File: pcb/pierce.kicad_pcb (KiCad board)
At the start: 2 copper layers, 227.3 x 105.6 mm, 100 parts, among them J1 Conn_01x12, J2 Conn_01x12, J3 Trackpoint, SW1 SW_PUSH, SW10 SW_PUSH, SW11 SW_PUSH, SW12 SW_PUSH, SW13 SW_PUSH, SW14 SW_PUSH, SW15 SW_PUSH, SW16 SW_PUSH, SW17 SW_PUSH, SW18 SW_PUSH, SW19 SW_PUSH, SW2 SW_PUSH, SW20 SW_PUSH, SW21 SW_PUSH, SW22 SW_PUSH, SW23 SW_PUSH, SW24 SW_PUSH, SW25 SW_PUSH, SW26 SW_PUSH, SW27 SW_PUSH, SW28 SW_PUSH, SW29 SW_PUSH, SW3 SW_PUSH, SW30 SW_PUSH, SW31 SW_PUSH, SW32 SW_PUSH, SW33 SW_PUSH, SW34 SW_PUSH, SW35 SW_PUSH, SW36 SW_PUSH, SW37 SW_PUSH, SW38 Rotary_Encoder, SW4 SW_PUSH, SW5 SW_PUSH, SW6 SW_PUSH, SW7 SW_PUSH, SW8 SW_PUSH, SW9 SW_PUSH, U1 Elite-C_reverse

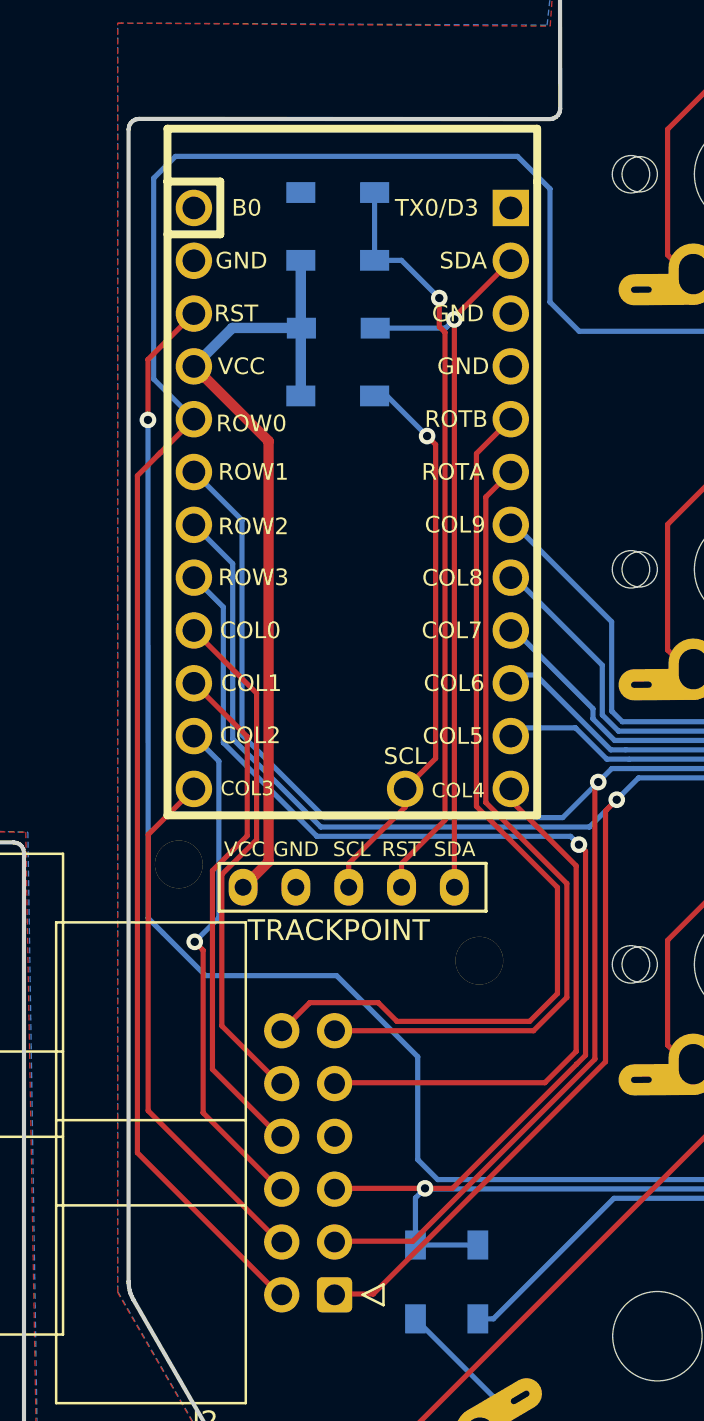
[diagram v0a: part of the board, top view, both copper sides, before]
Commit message: change pro micro footprint, smaller drill holes
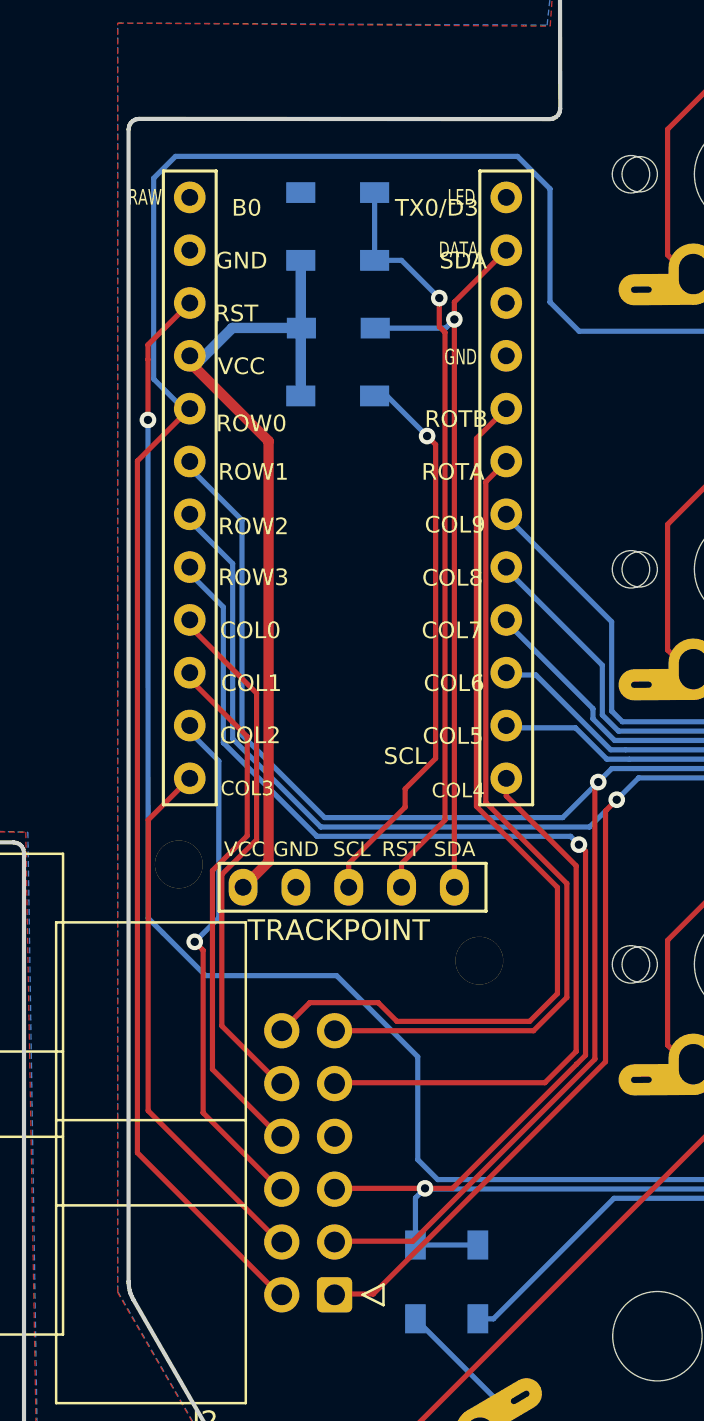
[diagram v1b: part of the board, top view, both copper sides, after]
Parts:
- U1: footprint pierce:Elite-C_reverse_D5 -> pierce:ProMicro_v2_1side
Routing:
- net col4: track 26.3 -> 26.9 mm
- net SDA: track 35.2 -> 35.8 mm

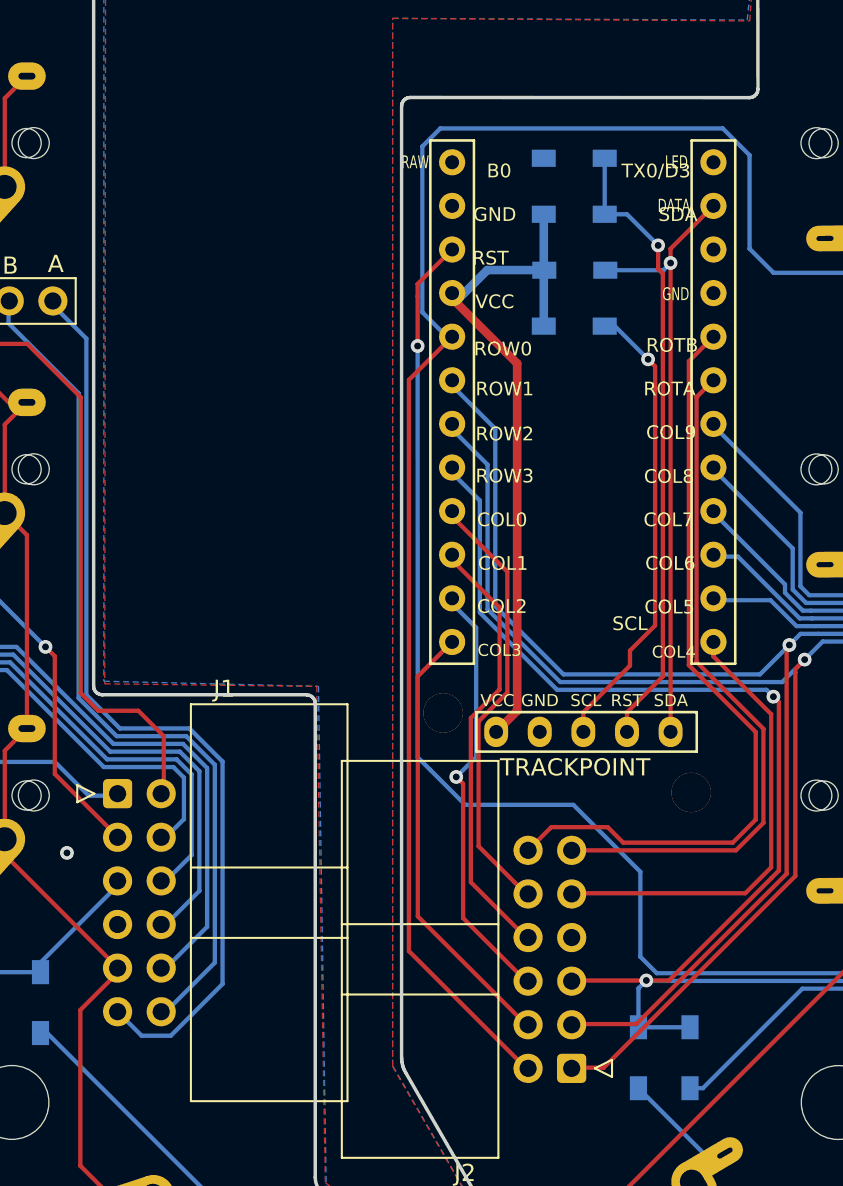
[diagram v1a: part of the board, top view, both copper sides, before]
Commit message: adjust schematics for wireless connection between halves
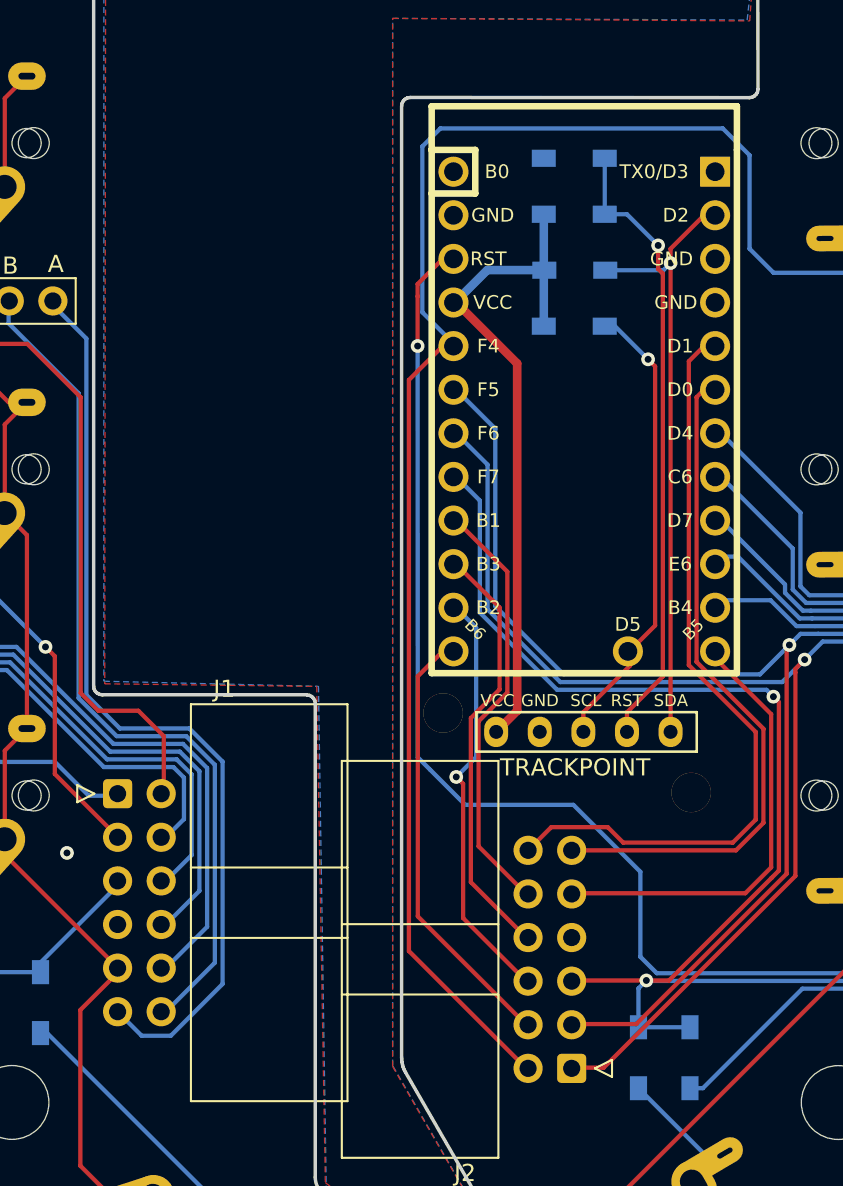
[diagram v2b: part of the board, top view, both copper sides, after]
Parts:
- U1: footprint pierce:ProMicro_v2_1side -> pierce:Elite-C_reverse_D5
- moved U1 0.13 mm to (157.5, 53.3)
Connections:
- U1 pad 1: (no net) -> Net-(U1-Pad1)
- U1 pad 24: (no net) -> Net-(U1-Pad24)

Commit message: place and route 2.0
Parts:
- removed D1, D10, D11, D12, D13, D14, D15, D16, D17, D18, D19, D2, D20, D21, D22, D23, D24, D25, D26, D27, D28, D29, D3, D30, D31, D32, D33, D34, D35, D36, D4, D5, D6, D7, D8, D9: D, kbd:D3_SMD_v2
- removed J1, J2: Conn_01x12, Connector_IDC:IDC-Header_2x06_P2.54mm_Horizontal
- removed J3: Trackpoint, pierce:TRACKPOINT
- removed the REF** at (62.9, 95.0)
- removed the REF** at (101.3, 26.0)
- removed the REF** at (63.4, 26.0)
- removed the Ref** at (53.7, 57.3)
- removed the Ref** at (219.1, 85.8)
- removed the Ref** at (149.5, 70.9)
- removed the Ref** at (162.6, 75.5)
- removed the Ref** at (53.7, 76.3)
- removed the Ref** at (110.6, 46.1)
- removed the Ref** at (124.4, 93.6)
- removed the Ref** at (77.8, 85.8)
- removed SW38: Rotary_Encoder, pierce:Rotary_encoder_conn
- added BT1: Device_Battery_Cell, pierce:BatteryHolder_Keystone_3034_1x20mm, B.Cu at (133.6, 85.5)
- added PROGL1: Conn_01x04_Male, pierce:PinHeader_1x04_P2.54mm_Horizontal, B.Cu at (139.4, 49.3)
- added PROGR1: Conn_01x04_Male, pierce:PinHeader_1x04_P2.54mm_Horizontal, B.Cu at (220.4, 84.3)
- added R4: 4k7, pierce:R_SMD_v2, B.Cu at (157.5, 51.5)
- added R5: 4k7, pierce:R_SMD_v2, B.Cu at (157.5, 48.2)
- added REF**: Breakaway_Tabs, kbd:Breakaway_Tabs, F.Cu at (41.2, 95.1)
- added REF**: Breakaway_Tabs, kbd:Breakaway_Tabs, F.Cu at (98.7, 26.0)
- added REF**: Breakaway_Tabs, kbd:Breakaway_Tabs, F.Cu at (60.8, 26.0)
- added REG1: LD1117S33TR_SOT223, Package_TO_SOT_SMD:SOT-223-3_TabPin2, B.Cu at (154.0, 90.6)
- added Ref**: Val**, pierce:OSHW-LOGO-M, B.Cu at (224.3, 91.2)
- added Ref**: Val**, pierce:OSHW-LOGO-M, F.Cu at (224.3, 91.2)
- added Ref**: Val**, kbd:M2_HOLE_v2, F.Cu at (51.1, 57.3)
- added Ref**: Val**, kbd:M2_HOLE_v2, F.Cu at (51.1, 76.3)
- added Ref**: Val**, kbd:M2_HOLE_v2, F.Cu at (108.1, 46.1)
- added Ref**: Val**, kbd:M2_HOLE_v2, F.Cu at (121.9, 93.6)
- added TP1: Trackpoint, pierce:TRACKPOINT, F.Cu at (152.1, 64.9)
- added YJL1: YJ-14015-NRF51822, pierce:YJ-14015, F.Cu at (135.9, 71.8)
- added YJR1: YJ-14015-NRF51822, pierce:YJ-14015, F.Cu at (167.2, 76.9)
- SW1, SW10, SW11, SW12, SW13, SW14, SW15, SW16, SW17, SW18, SW19, SW2, SW20, SW21, SW22, SW23, SW24, SW25, SW26, SW27, SW28, SW29, SW3, SW30, SW31, SW32, SW33, SW34, SW35, SW36, SW4, SW5, SW6, SW7, SW8, SW9: footprint kbd:keyswitch_cherrymx_alps_choc12_1u -> pierce:keyswitch_cherrymx_alps_choc12_1u
- moved AVR1 6.17 mm to (156.9, 47.2)
- moved R1 3.47 mm to (157.5, 35.1)
- moved C1 3.47 mm to (157.5, 38.4)
- moved R2 3.47 mm to (157.5, 44.9)
- moved R3 3.47 mm to (157.5, 41.7)
- moved SW33 2.54 mm to (130.2, 103.7)
- moved SW15 2.54 mm to (79.6, 33.0), turned to 0 degrees
- moved SW16 2.54 mm to (79.6, 52.0), turned to 0 degrees
- moved SW17 2.54 mm to (79.6, 71.0), turned to 0 degrees
- moved SW18 2.54 mm to (89.6, 93.1)
- moved SW23 2.54 mm to (98.6, 35.2), turned to 0 degrees
- moved SW24 2.54 mm to (98.6, 54.2), turned to 0 degrees
- moved SW25 2.54 mm to (98.6, 73.2), turned to 0 degrees
- moved SW30 2.54 mm to (117.6, 37.7), turned to 0 degrees
- moved SW31 2.54 mm to (117.6, 56.7), turned to 0 degrees
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- renumbered U1 to AVR1, SW37 to RST1
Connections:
- net VCC renamed VCC_R_5V
- AVR1 pad 10: col6 -> Net-(AVR1-Pad10)
- AVR1 pad 11: col5 -> Net-(AVR1-Pad11)
- AVR1 pad 12: col4 -> Net-(AVR1-Pad12)
- AVR1 pad 13: col3 -> Net-(AVR1-Pad13)
- AVR1 pad 14: col2 -> Net-(AVR1-Pad14)
- AVR1 pad 15: col1 -> Net-(AVR1-Pad15)
- AVR1 pad 16: col0 -> Net-(AVR1-Pad16)
- AVR1 pad 17: row3 -> Net-(AVR1-Pad17)
- AVR1 pad 18: row2 -> Net-(AVR1-Pad18)
- AVR1 pad 19: row1 -> Net-(AVR1-Pad19)
- AVR1 pad 20: row0 -> Net-(AVR1-Pad20)
- AVR1 pad 23: GND -> GND_R
- AVR1 pad 3: GND -> GND_R
- AVR1 pad 4: GND -> GND_R
- AVR1 pad 5: rotb -> I2C_SDA
- AVR1 pad 6: rota -> I2C_SCL
- AVR1 pad 7: col9 -> Net-(AVR1-Pad7)
- AVR1 pad 8: col8 -> Net-(AVR1-Pad8)
- AVR1 pad 9: col7 -> Net-(AVR1-Pad9)
- R1 pad 1: GND -> GND_R
- RST1 pad 2: GND -> GND_R
- SW1 pad 1: col0l -> GND_L
- SW1 pad 2: Net-(D1-Pad2) -> SW00L
- SW10 pad 1: col1l -> GND_L
- SW10 pad 2: Net-(D10-Pad2) -> SW21L
- SW11 pad 1: col6 -> GND_R
- SW11 pad 2: Net-(D11-Pad2) -> SW01R
- SW12 pad 1: col6 -> GND_R
- SW12 pad 2: Net-(D12-Pad2) -> SW11R
- SW13 pad 1: col6 -> GND_R
- SW13 pad 2: Net-(D13-Pad2) -> SW21R
- SW14 pad 1: col6 -> GND_R
- SW14 pad 2: Net-(D14-Pad2) -> SW31R
- SW15 pad 1: col2l -> GND_L
- SW15 pad 2: Net-(D15-Pad2) -> SW02L
- SW16 pad 1: col2l -> GND_L
- SW16 pad 2: Net-(D16-Pad2) -> SW12L
- SW17 pad 1: col2l -> GND_L
- SW17 pad 2: Net-(D17-Pad2) -> SW22L
- SW18 pad 1: col2l -> GND_L
- SW18 pad 2: Net-(D18-Pad2) -> SW32L
- SW19 pad 1: col7 -> GND_R
- SW19 pad 2: Net-(D19-Pad2) -> SW02R
- SW2 pad 1: col0l -> GND_L
- SW2 pad 2: Net-(D2-Pad2) -> SW10L
- SW20 pad 1: col7 -> GND_R
- SW20 pad 2: Net-(D20-Pad2) -> SW12R
- SW21 pad 1: col7 -> GND_R
- SW21 pad 2: Net-(D21-Pad2) -> SW22R
- SW22 pad 1: col7 -> GND_R
- SW22 pad 2: Net-(D22-Pad2) -> SW32R
- SW23 pad 1: col3l -> GND_L
- SW23 pad 2: Net-(D23-Pad2) -> SW03L
- SW24 pad 1: col3l -> GND_L
- SW24 pad 2: Net-(D24-Pad2) -> SW13L
- SW25 pad 1: col3l -> GND_L
- SW25 pad 2: Net-(D25-Pad2) -> SW23L
- SW26 pad 1: col3l -> GND_L
- SW26 pad 2: Net-(D26-Pad2) -> SW33L
- SW27 pad 1: col8 -> GND_R
- SW27 pad 2: Net-(D27-Pad2) -> SW03R
- SW28 pad 1: col8 -> GND_R
- SW28 pad 2: Net-(D28-Pad2) -> SW13R
- SW29 pad 1: col8 -> GND_R
- SW29 pad 2: Net-(D29-Pad2) -> SW23R
- SW3 pad 1: col0l -> GND_L
- SW3 pad 2: Net-(D3-Pad2) -> SW20L
- SW30 pad 1: col4l -> GND_L
- SW30 pad 2: Net-(D30-Pad2) -> SW04L
- SW31 pad 1: col4l -> GND_L
- SW31 pad 2: Net-(D31-Pad2) -> SW14L
- SW32 pad 1: col4l -> GND_L
- SW32 pad 2: Net-(D32-Pad2) -> SW24L
- SW33 pad 1: col4l -> GND_L
- SW33 pad 2: Net-(D33-Pad2) -> SW34L
- SW34 pad 1: col9 -> GND_R
- SW34 pad 2: Net-(D34-Pad2) -> SW04R
- SW35 pad 1: col9 -> GND_R
- SW35 pad 2: Net-(D35-Pad2) -> SW14R
- SW36 pad 1: col9 -> GND_R
- SW36 pad 2: Net-(D36-Pad2) -> SW24R
- SW4 pad 1: col5 -> GND_R
- SW4 pad 2: Net-(D4-Pad2) -> SW00R
- SW5 pad 1: col5 -> GND_R
- SW5 pad 2: Net-(D5-Pad2) -> SW10R
- SW6 pad 1: col5 -> GND_R
- SW6 pad 2: Net-(D6-Pad2) -> SW20R
- SW7 pad 1: col5 -> GND_R
- SW7 pad 2: Net-(D7-Pad2) -> SW30R
- SW8 pad 1: col1l -> GND_L
- SW8 pad 2: Net-(D8-Pad2) -> SW01L
- SW9 pad 1: col1l -> GND_L
- SW9 pad 2: Net-(D9-Pad2) -> SW11L
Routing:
- net GND_R: track 0.00 -> 522.9 mm, vias 0 -> 2
- net GND_L: track 0.00 -> 470.2 mm, vias 0 -> 2
- net row0: track 178.6 -> 0.00 mm
- net row2: track 163.2 -> 0.00 mm, vias 1 -> 0
- net row1: track 161.8 -> 0.00 mm, vias 3 -> 0
- net col0l: track 155.7 -> 0.00 mm, vias 1 -> 0
- net col9: track 150.3 -> 0.00 mm, vias 1 -> 0
- net col7: track 137.0 -> 0.00 mm, vias 1 -> 0
- net col2l: track 132.2 -> 0.00 mm, vias 1 -> 0
- net col1l: track 129.7 -> 0.00 mm, vias 1 -> 0
- net VCC_R_3.3V: track 0.00 -> 128.6 mm, vias 0 -> 2
- net SW04R: track 0.00 -> 127.7 mm
- net col8: track 127.0 -> 0.00 mm, vias 1 -> 0
- net row0l: track 122.5 -> 0.00 mm, vias 1 -> 0
- net col6: track 121.2 -> 0.00 mm, vias 1 -> 0
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- removed copper zone on B.Cu, net GND
- removed copper zone on F.Cu, net GND
- removed copper zone on B.Cu, net GND1
- removed copper zone on F.Cu, net GND1
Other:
- board size 227.3 x 105.6 mm -> 229.8 x 105.7 mm
- board text added: "3.3V"
- board text added: "CLK"
- board text added: "DIO"
- board text added: "Pierce 2.0"
- board text added: "by durken"
- board text removed: "A"
- board text removed: "B"
- board text removed: "C"
- board text removed: "COL0"
- board text removed: "COL1"
- board text removed: "COL2"
- board text removed: "COL3"
- board text removed: "COL4"
- board text removed: "COL5"
- board text removed: "COL6"
- board text removed: "COL7"
- board text removed: "COL8"
- board text removed: "Pierce 1.1"
- board text removed: "ROW0"
- board text removed: "ROW1"
- board text removed: "ROW2"
- board text removed: "ROW3"
